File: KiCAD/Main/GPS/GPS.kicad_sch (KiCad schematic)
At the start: 7 parts, among them J8 Conn_Coaxial, U5 MAX-M8Q

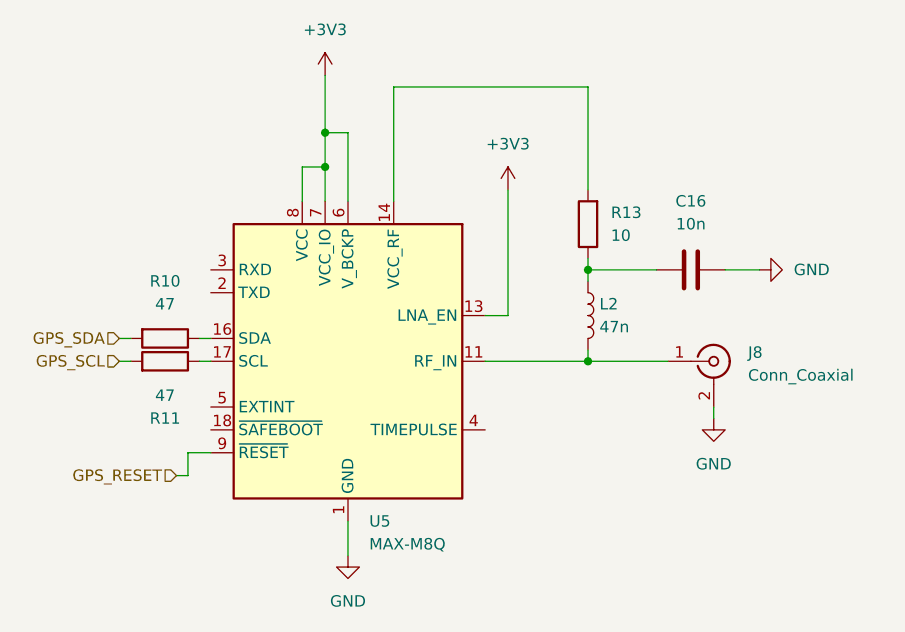
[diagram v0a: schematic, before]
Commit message: Update aux magnetometer, test THs, and silkscreens
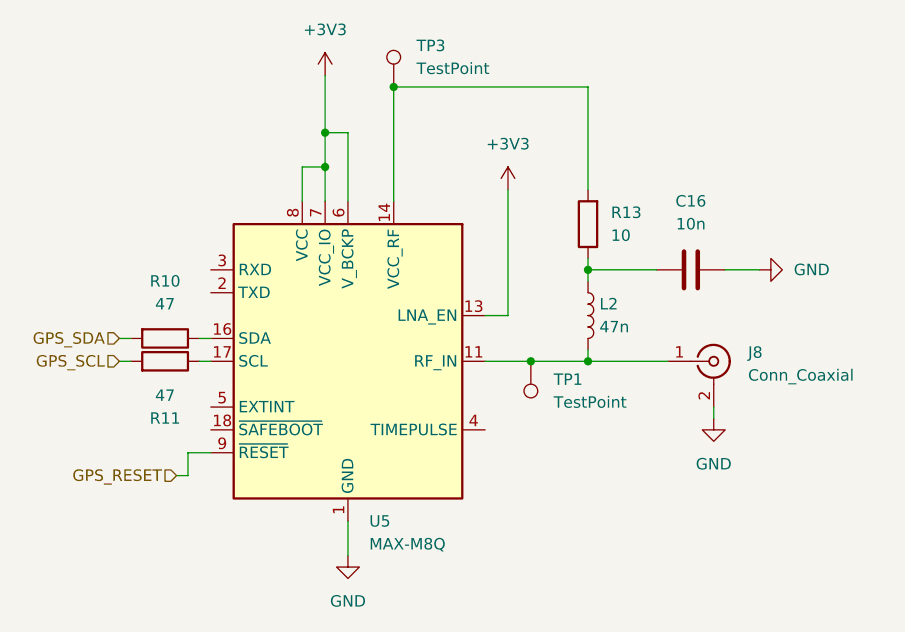
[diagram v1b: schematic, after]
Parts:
- added TP1, TP3: TestPoint, TestPoint:TestPoint_THTPad_1.5x1.5mm_Drill0.7mm, symbol Connector:TestPoint
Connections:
- net at J8.1 (In), L2.2, U5.11 (RF_IN): now also TP1.1
- net at R13.2, U5.14 (VCC_RF): now also TP3.1
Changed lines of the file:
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@@
+	)
+	(junction
+		(at 119.38 106.68)
+		(diameter 0)
+		(color 0 0 0 0)
+	)
+	(junction
+		(at 104.14 76.2)
+		(diameter 0)
+		(color 0 0 0 0)
 	)
 	(junction
@@
 	(wire
 		(pts
-			(xy 114.3 106.68) (xy 125.73 106.68)
+			(xy 114.3 106.68) (xy 119.38 106.68)
+		)
+		(stroke
+			(width 0)
+			(type default)
+		)
+	)
+	(wire
+		(pts
+			(xy 104.14 76.2) (xy 125.73 76.2)
 		)
 		(stroke
@@
 	(wire
 		(pts
-			(xy 125.73 76.2) (xy 104.14 76.2)
-		)
-		(stroke
-			(width 0)
-			(type default)
-		)
-	)
-	(wire
-		(pts
 			(xy 104.14 76.2) (xy 104.14 88.9)
 		)
@@
 		(pts
 			(xy 93.98 88.9) (xy 93.98 85.09)
+		)
+		(stroke
+			(width 0)
+			(type default)
+		)
+	)
+	(wire
+		(pts
+			(xy 119.38 106.68) (xy 125.73 106.68)
 		)
 		(stroke
@@
 	)
 	(symbol
+		(lib_id "Connector:TestPoint")
+		(at 119.38 106.68 180)
+		(unit 1)
+		(exclude_from_sim no)
+		(in_bom yes)
+		(on_board yes)
+		(dnp no)
+		(fields_autoplaced yes)
+		(property "Reference" "TP1"
+			(at 121.92 108.7119 0)
+			(effects
+				(font
+					(size 1.27 1.27)
+				)
+				(justify right)
+			)
+		)
+		(property "Value" "TestPoint"
+			(at 121.92 111.2519 0)
+			(effects
+				(font
+					(size 1.27 1.27)
+				)
+				(justify right)
+			)
+		)
+		(property "Footprint" "TestPoint:TestPoint_THTPad_1.5x1.5mm_Drill0.7mm"
+			(at 114.3 106.68 0)
+			(effects
+				(font
+					(size 1.27 1.27)
+				)
+				(hide yes)
+			)
+		)
+		(property "Datasheet" "~"
+			(at 114.3 106.68 0)
+			(effects
+				(font
+					(size 1.27 1.27)
+				)
+				(hide yes)
+			)
+		)
+		(property "Description" "test point"
+			(at 119.38 106.68 0)
+			(effects
+				(font
+					(size 1.27 1.27)
+				)
+				(hide yes)
+			)
+		)
+		(pin "1"
+		)
+		(instances
+			(project ""
+				(path "/bbb10697-a5dd-43b8-9c6f-4c5919cf3463/aff6795e-9a09-4ffe-99fb-dba81cca4540"
+					(reference "TP1")
+					(unit 1)
+				)
+			)
+		)
+	)
+	(symbol
 		(lib_id "RF_GPS:MAX-M8Q")
 		(at 99.06 106.68 0)
@@
 					(unit 1)
 				)
+			)
+		)
+	)
+	(symbol
+		(lib_id "Connector:TestPoint")
+		(at 104.14 76.2 0)
+		(unit 1)
+		(exclude_from_sim no)
+		(in_bom yes)
+		(on_board yes)
+		(dnp no)
+		(fields_autoplaced yes)
+		(property "Reference" "TP3"
+			(at 106.68 71.6279 0)
+			(effects
+				(font
+					(size 1.27 1.27)
+				)
+				(justify left)
+			)
+		)
+		(property "Value" "TestPoint"
+			(at 106.68 74.1679 0)
+			(effects
+				(font
+					(size 1.27 1.27)
+				)
+				(justify left)
+			)
+		)
+		(property "Footprint" "TestPoint:TestPoint_THTPad_1.5x1.5mm_Drill0.7mm"
+			(at 109.22 76.2 0)
+			(effects
+				(font
+					(size 1.27 1.27)
+				)
+				(hide yes)
+			)
+		)
+		(property "Datasheet" "~"
+			(at 109.22 76.2 0)
+			(effects
+				(font
+					(size 1.27 1.27)
+				)
+				(hide yes)
+			)
+		)
+		(property "Description" "test point"
+			(at 104.14 76.2 0)
+			(effects
+				(font
+					(size 1.27 1.27)
+				)
+				(hide yes)
+			)
+		)
+		(pin "1"
+		)
+		(instances
+			(project "Main"
+				(path "/bbb10697-a5dd-43b8-9c6f-4c5919cf3463/aff6795e-9a09-4ffe-99fb-dba81cca4540"
+					(reference "TP3")
+					(unit 1)
+				)
